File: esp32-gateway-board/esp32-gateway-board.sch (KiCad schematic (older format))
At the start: 3 parts

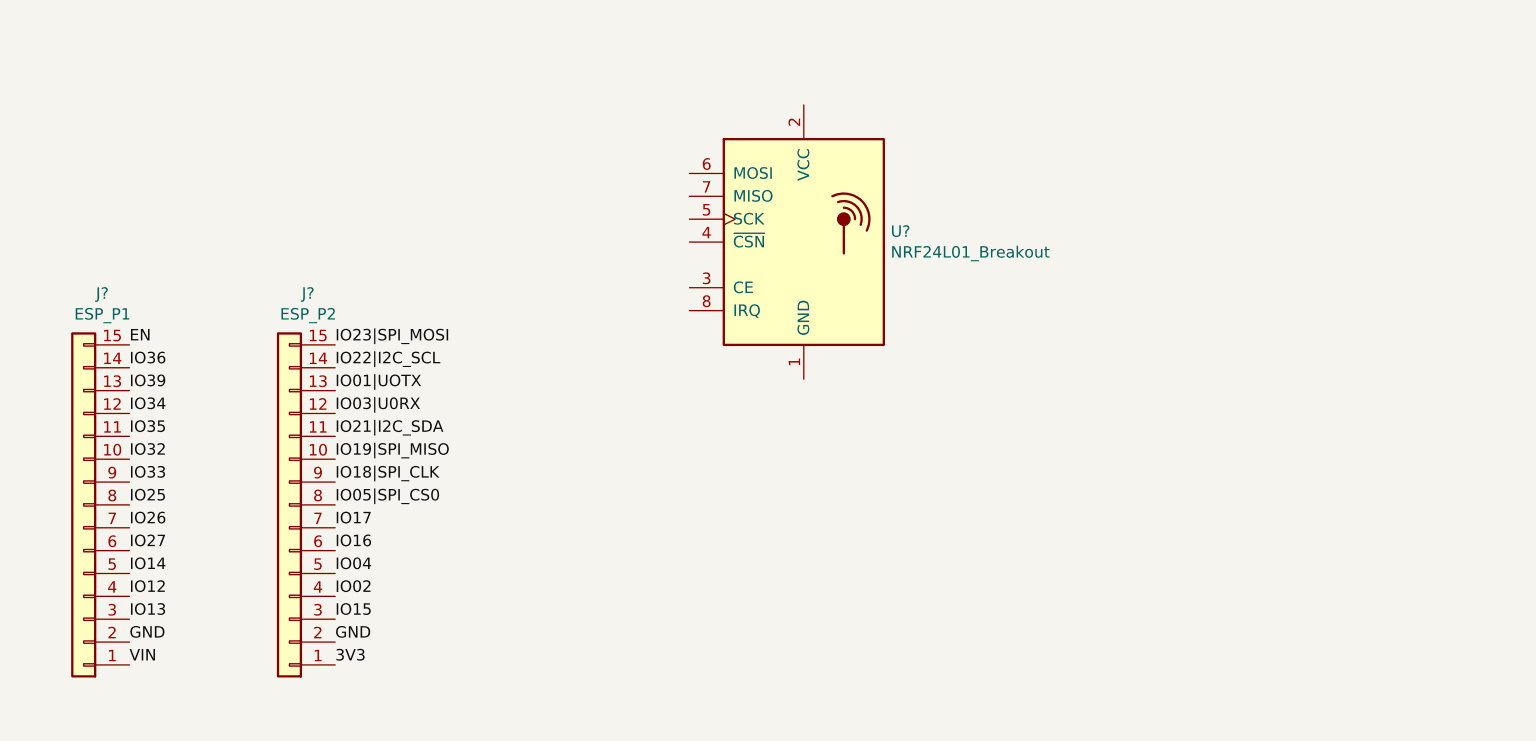
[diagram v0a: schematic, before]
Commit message: esp32 gateway with pcb
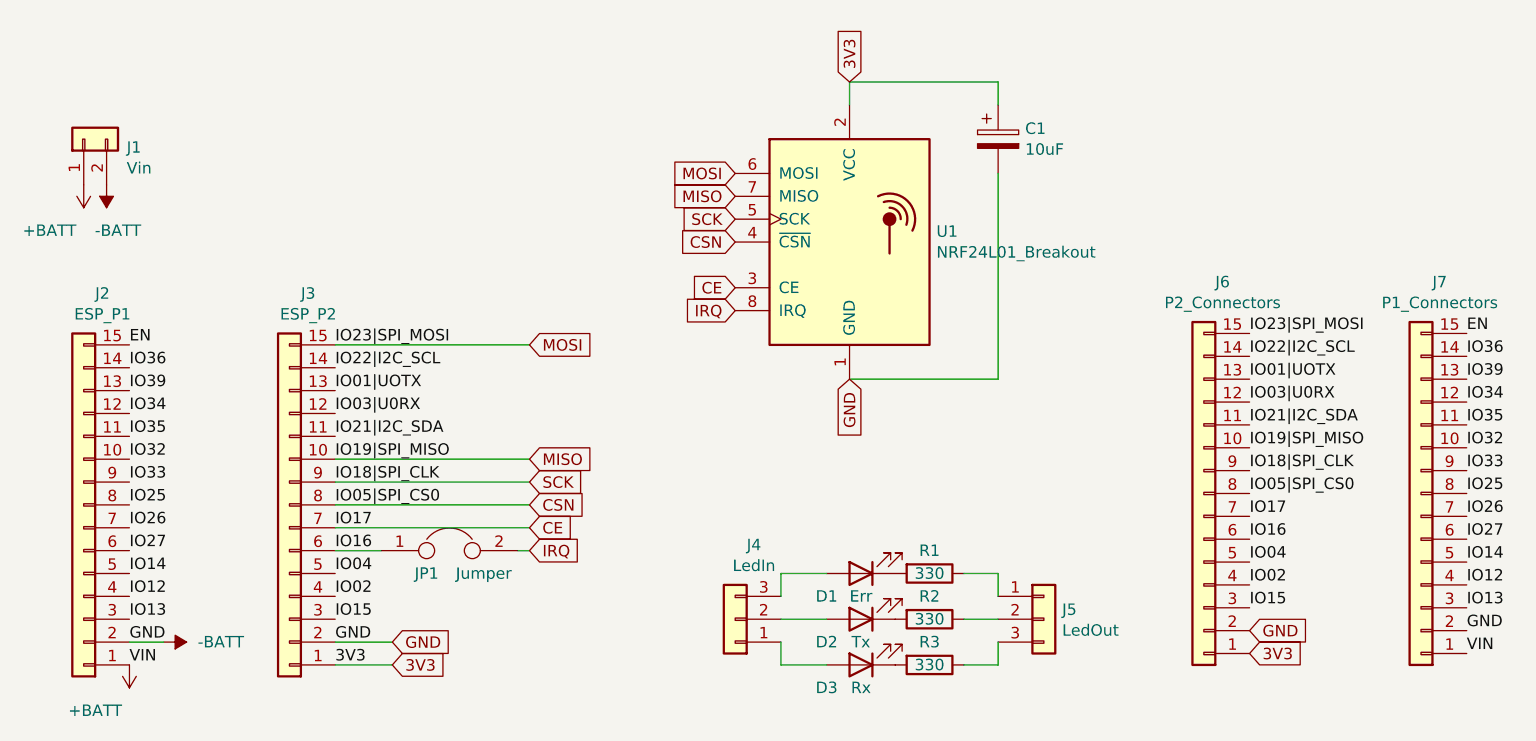
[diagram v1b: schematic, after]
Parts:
- added C1: 10uF, Connector_PinSocket_2.54mm:PinSocket_1x02_P2.54mm_Vertical, symbol Device:CP
- added D1: Err, LED_THT:LED_D3.0mm, symbol Device:LED
- added D2: Tx, LED_THT:LED_D3.0mm, symbol Device:LED
- added D3: Rx, LED_THT:LED_D3.0mm, symbol Device:LED
- added J1: Vin, Connector_PinSocket_2.54mm:PinSocket_1x02_P2.54mm_Vertical, symbol Connector_Generic:Conn_01x02
- added J4: LedIn, Connector_PinSocket_2.54mm:PinSocket_1x03_P2.54mm_Vertical, symbol Connector_Generic:Conn_01x03
- added J5: LedOut, Connector_PinSocket_2.54mm:PinSocket_1x03_P2.54mm_Vertical, symbol Connector_Generic:Conn_01x03
- added J6: P2_Connectors, Connector_PinSocket_2.54mm:PinSocket_1x15_P2.54mm_Vertical, symbol Connector_Generic:Conn_01x15
- added J7: P1_Connectors, Connector_PinSocket_2.54mm:PinSocket_1x15_P2.54mm_Vertical, symbol Connector_Generic:Conn_01x15
- added JP1: Jumper, Connector_PinHeader_2.54mm:PinHeader_1x02_P2.54mm_Vertical, symbol Device:Jumper
- added R1, R2, R3: 330, Resistor_THT:R_Axial_DIN0207_L6.3mm_D2.5mm_P10.16mm_Horizontal, symbol Device:R
- J2, J3: renamed from J?; footprint (none) -> Connector_PinSocket_2.54mm:PinSocket_1x15_P2.54mm_Vertical
- gave numbers to parts that had none: 1
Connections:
- net GND is gone; now on net -BATT: J2.2 (Pin_2), J3.2 (Pin_2)
- net IO05|SPI_CS0 is gone; now on net CSN: J3.8 (Pin_8)
- net IO17 is gone; now on net CE: J3.7 (Pin_7)
- net IO18|SPI_CLK is gone; now on net SCK: J3.9 (Pin_9)
- net IO19|SPI_MISO is gone; now on net MISO: J3.10 (Pin_10)
- net IO23|SPI_MOSI is gone; now on net MOSI: J3.15 (Pin_15)
- net 3V3: now also U1.2 (VCC), C1.1, J6.1 (Pin_1)
- net EN: now also J7.15 (Pin_15)
- net IO01|UOTX: now also J6.13 (Pin_13)
- net IO02: now also J6.4 (Pin_4)
- net IO03|U0RX: now also J6.12 (Pin_12)
- net IO04: now also J6.5 (Pin_5)
- net IO12: now also J7.4 (Pin_4)
- net IO13: now also J7.3 (Pin_3)
- net IO14: now also J7.5 (Pin_5)
- net IO15: now also J6.3 (Pin_3)
- net IO16: now also J6.6 (Pin_6), JP1.1
- net IO21|I2C_SDA: now also J6.11 (Pin_11)
- net IO22|I2C_SCL: now also J6.14 (Pin_14)
- net IO25: now also J7.8 (Pin_8)
- net IO26: now also J7.7 (Pin_7)
- net IO27: now also J7.6 (Pin_6)
- net IO32: now also J7.10 (Pin_10)
- net IO33: now also J7.9 (Pin_9)
- net IO34: now also J7.12 (Pin_12)
- net IO35: now also J7.11 (Pin_11)
- net IO36: now also J7.14 (Pin_14)
- net IO39: now also J7.13 (Pin_13)
- net -BATT: now reaches U1.1 (GND)
- net -BATT: now also C1.2, J1.2 (Pin_2), J6.2 (Pin_2), J7.2 (Pin_2)
- net CE: now reaches U1.3 (CE)
- net CE: now also J6.7 (Pin_7)
- net CSN: now reaches U1.4 (~CSN)
- net CSN: now also J6.8 (Pin_8)
- net SCK: now reaches U1.5 (SCK)
- net SCK: now also J6.9 (Pin_9)
- net MOSI: now reaches U1.6 (MOSI)
- net MOSI: now also J6.15 (Pin_15)
- net MISO: now reaches U1.7 (MISO)
- net MISO: now also J6.10 (Pin_10)
- net IRQ: now reaches U1.8 (IRQ)
- net IRQ: now also JP1.2
- net VIN renamed +BATT
- net +BATT: now also J1.1 (Pin_1), J7.1 (Pin_1)
- new net: D1.1 (K), R1.2
- new net: D1.2 (A), J4.3 (Pin_3)
- new net: D2.1 (K), R2.2
- new net: D2.2 (A), J4.2 (Pin_2)
- new net: D3.1 (K), R3.2
- new net: D3.2 (A), J4.1 (Pin_1)
- new net: J5.1 (Pin_1), R1.1
- new net: J5.2 (Pin_2), R2.1
- new net: J5.3 (Pin_3), R3.1
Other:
- moved on the sheet: U1

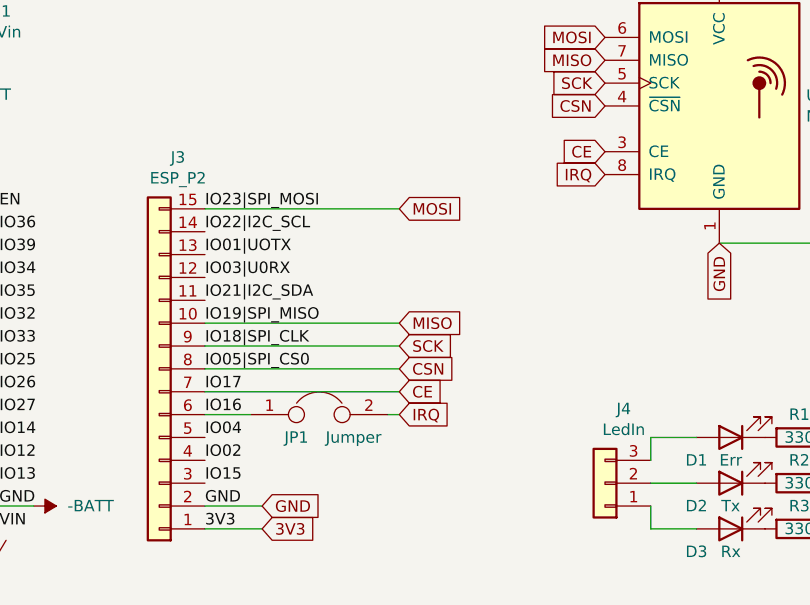
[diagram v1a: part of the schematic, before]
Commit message: update schematic
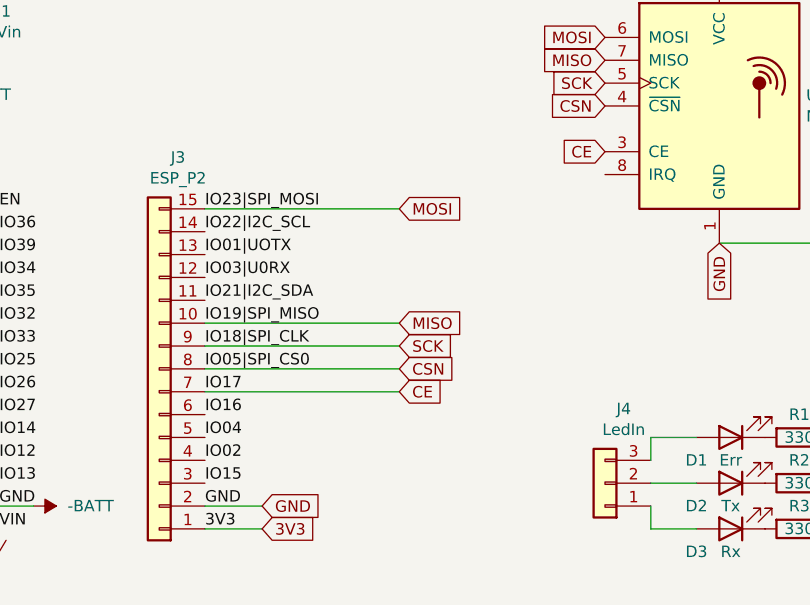
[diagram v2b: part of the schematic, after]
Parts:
- removed JP1: Jumper, Connector_PinHeader_2.54mm:PinHeader_1x02_P2.54mm_Vertical, symbol Device:Jumper
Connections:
- net IRQ: no longer names the net of U1.8 (IRQ)
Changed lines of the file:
@@
 Wire Wire Line
 	4200 2550 5050 2550
-Text GLabel 5950 1700 0    50   Input ~ 0
-IRQ
-Text GLabel 5050 2750 2    50   Input ~ 0
-IRQ
-Wire Wire Line
-	4200 2750 4400 2750
 Text GLabel 4450 3250 2    50   Input ~ 0
 3V3
@@
 GND
 $Comp
-L Device:Jumper JP1
-U 1 1 5F556D09
-P 4700 2750
-F 0 "JP1" H 4600 2650 50  0000 C CNN
-F 1 "Jumper" H 4850 2650 50  0000 C CNN
-F 2 "Connector_PinHeader_2.54mm:PinHeader_1x02_P2.54mm_Vertical" H 4700 2750 50  0001 C CNN
-F 3 "~" H 4700 2750 50  0001 C CNN
-	1    4700 2750
-	1    0    0    -1
-$EndComp
-Wire Wire Line
-	5000 2750 5050 2750
-$Comp
 L Device:LED D1
